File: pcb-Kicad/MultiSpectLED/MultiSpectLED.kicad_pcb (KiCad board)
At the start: 2 copper layers, 113.4 x 56 mm, 102 parts, among them J1 Conn_01x02_Female, J2 USB_C_Receptacle_USB2.0, SW1 NKK_HEXADEC, SW2 NKK_HEXADEC, U1 PAM2804, U10 PAM2804, U11 PAM2804, U12 PAM2804, U13 PAM2804, U14 PAM2804, U15 PAM2804, U16 PAM2804, U2 TeensyLC, U3 PAM2804, U4 PAM2804, U5 PAM2804, U6 PAM2804, U7 PAM2804, U8 PAM2804, U9 PAM2804

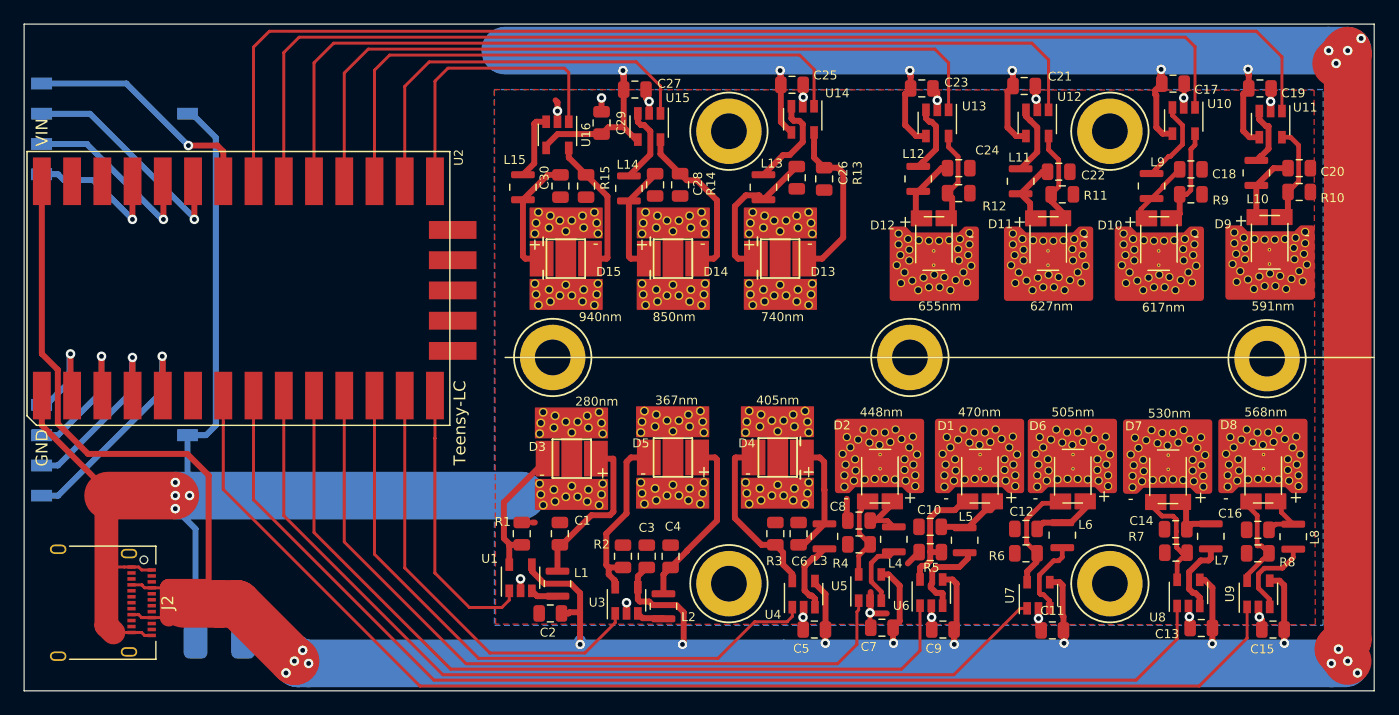
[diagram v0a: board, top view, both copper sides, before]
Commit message: Added pulldown resistors on each PAM2804 enable line
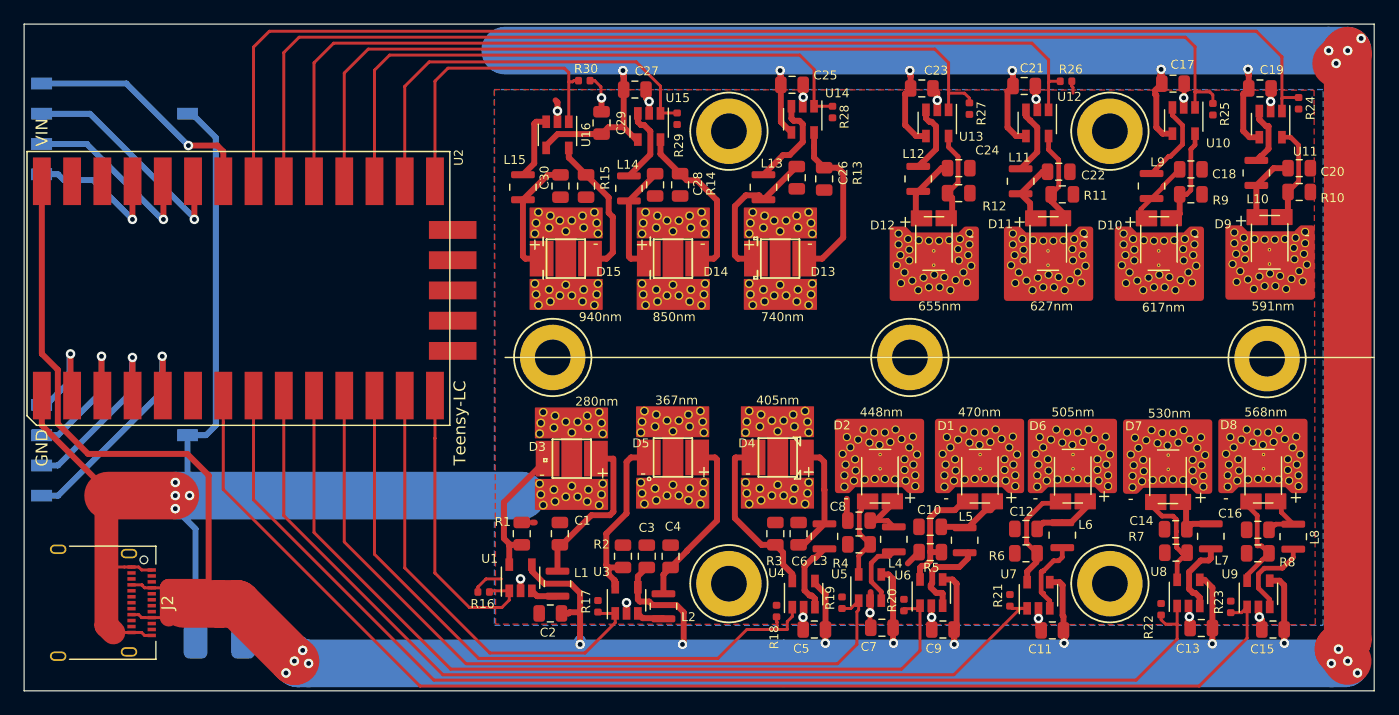
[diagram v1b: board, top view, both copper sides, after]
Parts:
- added R16: 100K, MultiSpectLED:R_0402_1005Metric, F.Cu at (162.2, 112.7)
- added R17: 100K, MultiSpectLED:R_0402_1005Metric, F.Cu at (171.8, 113.9)
- added R18: 100K, MultiSpectLED:R_0402_1005Metric, F.Cu at (186.8, 114.3)
- added R19: 100K, MultiSpectLED:R_0402_1005Metric, F.Cu at (192.3, 113.6)
- added R20: 100K, MultiSpectLED:R_0402_1005Metric, F.Cu at (197.5, 113.8)
- added R21: 100K, MultiSpectLED:R_0402_1005Metric, F.Cu at (206.4, 113.4)
- added R22: 100K, MultiSpectLED:R_0402_1005Metric, F.Cu at (219.1, 114.2)
- added R23: 100K, MultiSpectLED:R_0402_1005Metric, F.Cu at (224.9, 114.0)
- added R24: 100K, MultiSpectLED:R_0402_1005Metric, F.Cu at (230.7, 71.7)
- added R25: 100K, MultiSpectLED:R_0402_1005Metric, F.Cu at (223.4, 72.2)
- added R26: 100K, MultiSpectLED:R_0402_1005Metric, F.Cu at (211.1, 69.8)
- added R27: 100K, MultiSpectLED:R_0402_1005Metric, F.Cu at (203.0, 72.1)
- added R28: 100K, MultiSpectLED:R_0402_1005Metric, F.Cu at (191.5, 72.4)
- added R29: 100K, MultiSpectLED:R_0402_1005Metric, F.Cu at (178.4, 73.0)
- added R30: 100K, MultiSpectLED:R_0402_1005Metric, F.Cu at (170.7, 69.8)
- L1, L10, L11, L12, L13, L14, L15, L2, L3, L4, L5, L6, L7, L8, L9: value L -> 4.7u
- R1, R10, R11, R12, R13, R14, R15, R2, R3, R4, R5, R6, R7, R8, R9: value R -> 0.2
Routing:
- net /GND: track 144.0 -> 148.0 mm
- net /PWM_D12_655nm: track 65.1 -> 67.4 mm
- net /PWM_D10_617nm: track 93.3 -> 95.6 mm
- net /PWM_D7_530nm: track 96.8 -> 98.7 mm
- net /PWM_D3_280nm: track 23.4 -> 25.1 mm
- net /PWM_D2_448nm: track 64.1 -> 65.7 mm
- net /PWM_D8_568nm: track 105.0 -> 106.6 mm
- net /PWM_D13_740nm: track 50.4 -> 51.9 mm
- net /PWM_D6_505nm: track 80.4 -> 81.9 mm
- net /PWM_D5_367nm: track 36.9 -> 38.4 mm
- net /PWM_D4_405nm: track 54.3 -> 55.8 mm
- net /PWM_D1_470nm: track 71.6 -> 73.0 mm
- net /PWM_D9_591nm: track 103.6 -> 105.1 mm
- net /PWM_D14_850nm: track 33.4 -> 34.8 mm
- net /PWM_D11_627nm: track 77.1 -> 78.1 mm
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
